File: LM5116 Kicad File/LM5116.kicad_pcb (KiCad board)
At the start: 4 copper layers, 58.5 x 83.3 mm, 84 parts, among them J1 XT60-M, J10 PH1-01-UA, J11 PH1-01-UA, J12 PH1-01-UA, J13 PH1-01-UA, J14 61300311121, J15 61300311121, J16 61300311121, J17 61300311121, J18 61300311121, J19 61300311121, J2 PH1-01-UA, J20 61300311121, J21 61300311121, J22 61300311121, J23 61300311121, J24 61300311121, J25 61300311121, J3 PH1-01-UA, J4 PH1-01-UA, J5 PH1-01-UA, J6 PH1-01-UA, J7 PH1-01-UA, J8 PH1-01-UA, J9 PH1-01-UA, Q1 CSD17304Q3, Q2 CSD17304Q3, Q3 CSD17304Q3, Q4 CSD17304Q3, Q5 2N7002, Q6 IQDH29NE2LM5CG, U1 LM25116MHX/NOPB, U2 TLV1701AIDBVR, U3 TL431DBZ

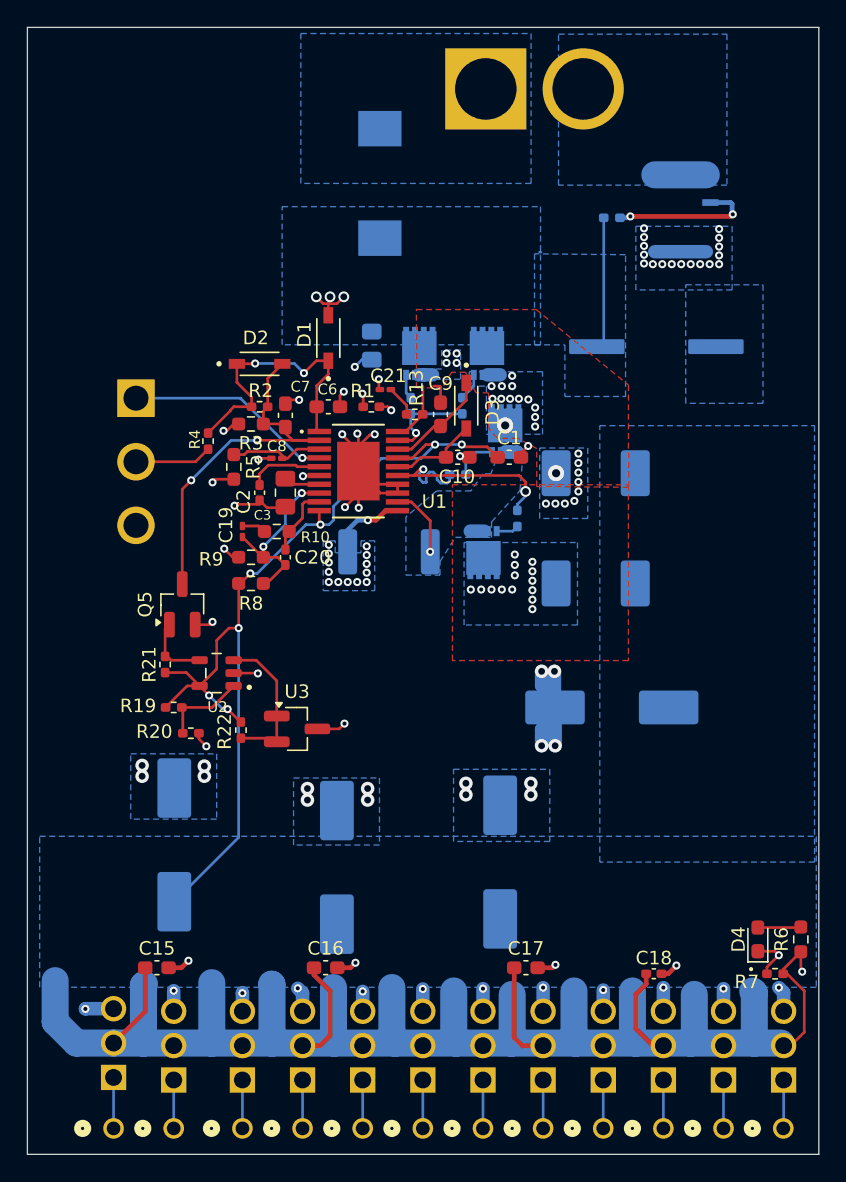
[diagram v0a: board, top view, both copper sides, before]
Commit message: Update Adding pulldown resistor
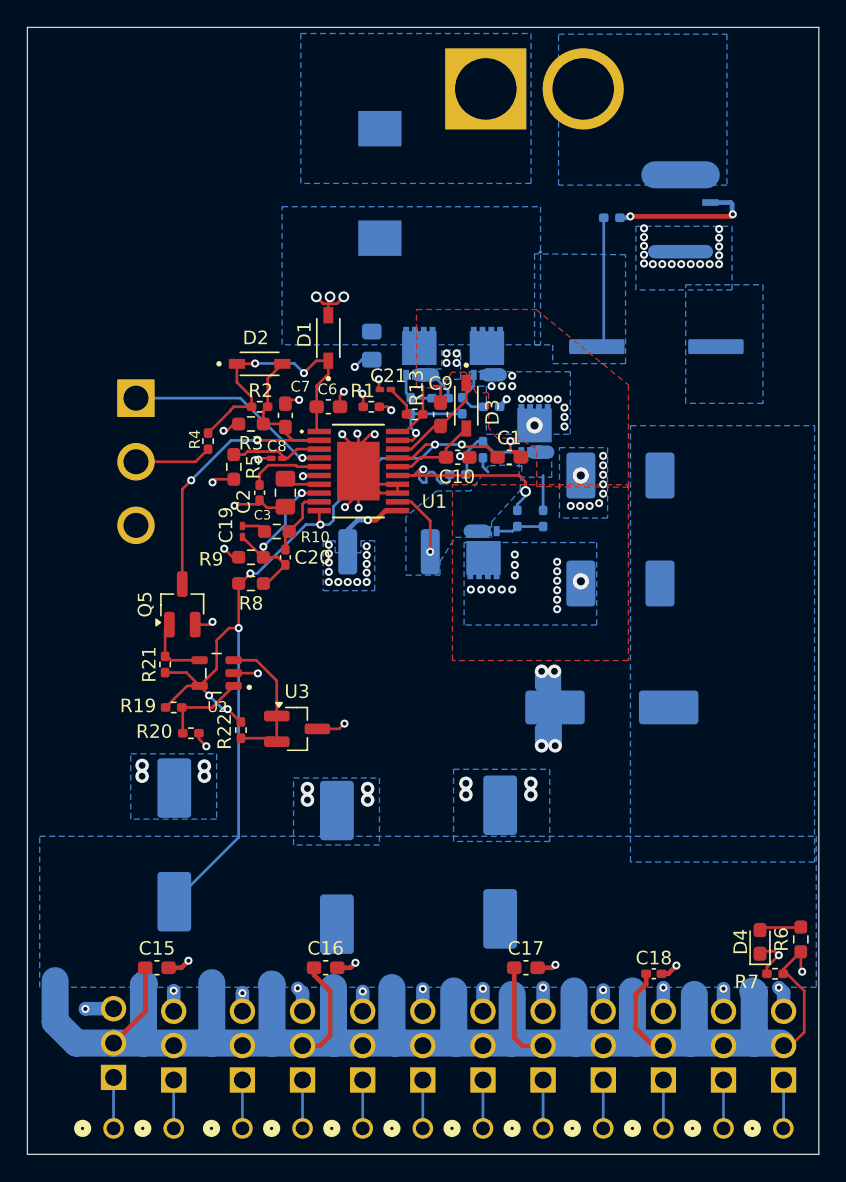
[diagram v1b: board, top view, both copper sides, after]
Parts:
- added R24: 10k, Resistor_SMD:R_0402_1005Metric_Pad0.72x0.64mm_HandSolder, B.Cu at (151.1, 72.4)
- added R25: 10k, Resistor_SMD:R_0402_1005Metric_Pad0.72x0.64mm_HandSolder, B.Cu at (147.3, 71.8)
- added R26: 10k, Resistor_SMD:R_0402_1005Metric_Pad0.72x0.64mm_HandSolder, B.Cu at (154.9, 80.6)
- added R27: 10k, Resistor_SMD:R_0402_1005Metric_Pad0.72x0.64mm_HandSolder, B.Cu at (150.5, 75.6)
- moved Q4 2.17 mm to (154.3, 74.2)
- moved L1 1.84 mm to (160.7, 77.5)
- moved L2 1.83 mm to (160.7, 85.5)
- moved D4 0.24 mm to (171.0, 111.9)
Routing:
- net /CS: track 7.91 -> 11.8 mm
- net Net-(Q4-Gate): track 3.15 -> 6.36 mm
- net /SW: track 8.15 -> 11.1 mm, vias 41 -> 43
- net Net-(Q3-Gate): track 1.67 -> 3.57 mm
- net Net-(Q1-Gate): track 2.04 -> 3.88 mm
- net Net-(Q2-Gate): track 1.83 -> 3.41 mm
- net GND: track 21.1 -> 21.9 mm
